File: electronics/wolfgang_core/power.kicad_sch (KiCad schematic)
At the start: 95 parts, among them IC1 LM5157RTER, J1 Power Supply, J2 Battery, J3 VXO7803-500-M-TR / ROF-78E3.3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, J4 VXO7805-500-M-TR / ROF-78E5.0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, Q1 SUM110P06-08L-E3, Q2 SUM110P06-08L-E3, Q3 SUM110P06-08L-E3, Q4 SUM110P06-08L-E3, Q5 BSS138P,215, Q6 IPD068P03L3GATMA1, SW1 power_switch, U1 LM5001MA, U2 ACS724xLCTR-50AB, U3 LTC4418IUF-PBF, U4 SN74AHCT1G08

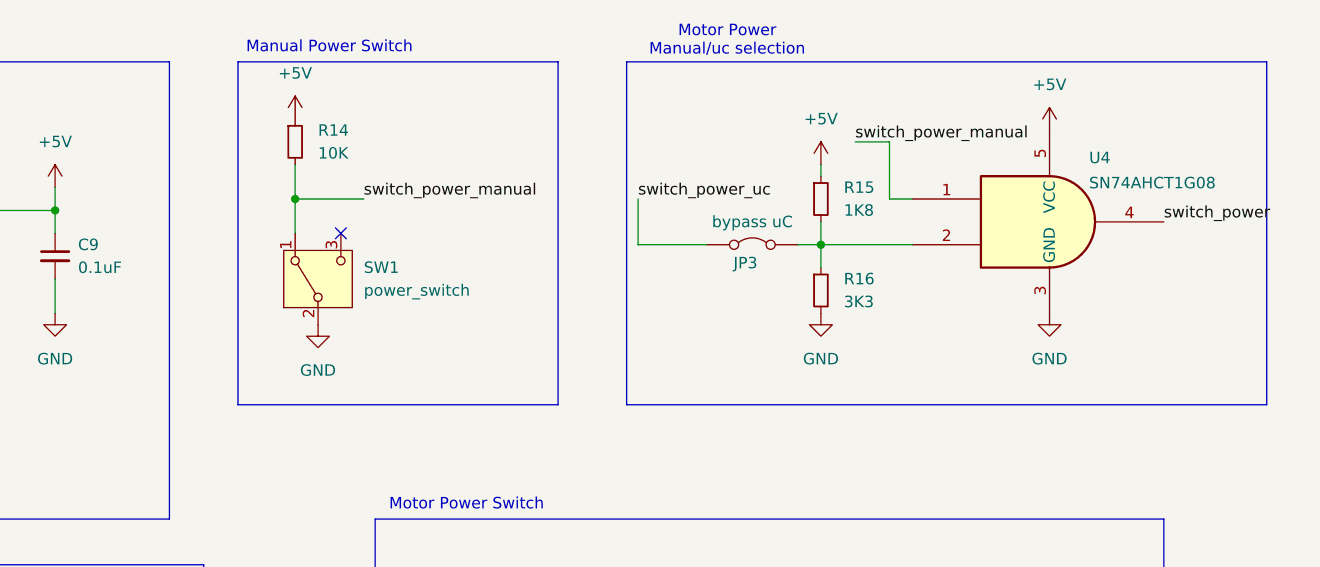
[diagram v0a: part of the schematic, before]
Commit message: Add ESP32 in io
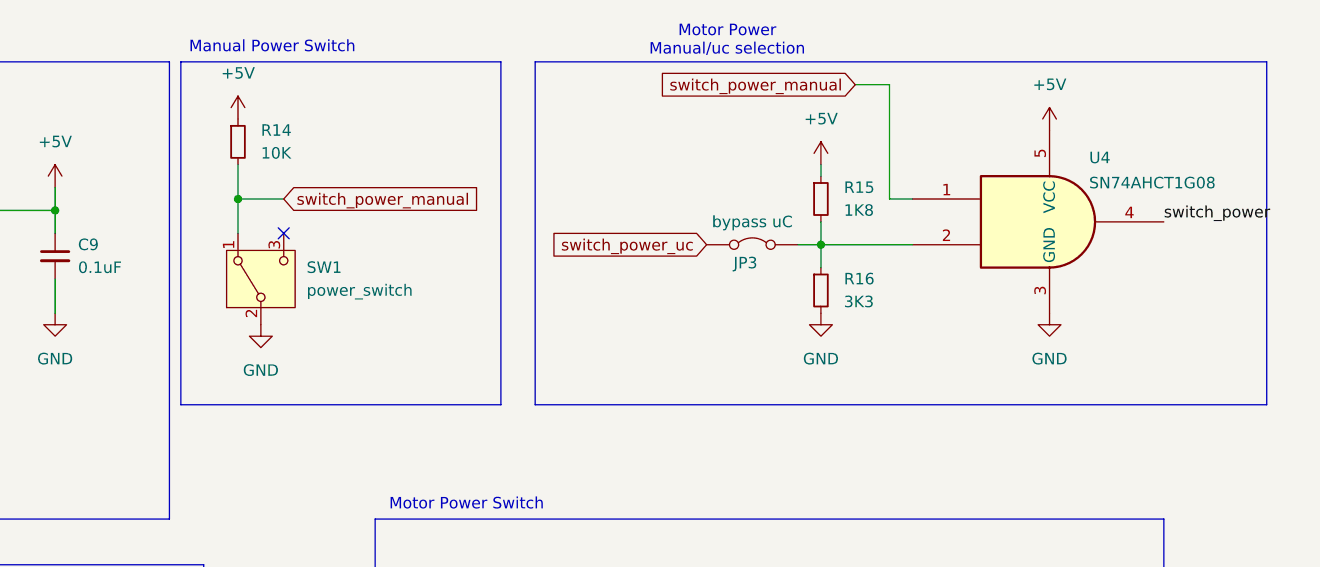
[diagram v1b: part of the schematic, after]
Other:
- moved on the sheet: R14, SW1
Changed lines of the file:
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@@
 	)
 	(junction
-		(at 293.37 33.02)
+		(at 287.02 33.02)
 		(diameter 0)
 		(color 0 0 0 0)
@@
 	)
 	(no_connect
-		(at 298.45 36.83)
+		(at 292.1 36.83)
 	)
 	(wire
@@
 	(wire
 		(pts
-			(xy 359.41 26.67) (xy 359.41 33.02)
+			(xy 359.41 20.32) (xy 359.41 33.02)
 		)
 		(stroke
@@
 	(wire
 		(pts
-			(xy 293.37 33.02) (xy 300.99 33.02)
+			(xy 287.02 33.02) (xy 292.1 33.02)
 		)
 		(stroke
@@
 	(wire
 		(pts
-			(xy 293.37 33.02) (xy 293.37 36.83)
+			(xy 287.02 33.02) (xy 287.02 36.83)
 		)
 		(stroke
@@
 	(wire
 		(pts
-			(xy 293.37 29.21) (xy 293.37 33.02)
+			(xy 287.02 29.21) (xy 287.02 33.02)
 		)
 		(stroke
@@
 	(wire
 		(pts
-			(xy 355.6 26.67) (xy 359.41 26.67)
+			(xy 355.6 20.32) (xy 359.41 20.32)
 		)
 		(stroke
@@
 	(wire
 		(pts
-			(xy 331.47 33.02) (xy 331.47 38.1)
-		)
-		(stroke
-			(width 0)
-			(type default)
-		)
-	)
-	(wire
-		(pts
 			(xy 140.97 240.03) (xy 140.97 241.3)
 		)
@@
 	(wire
 		(pts
-			(xy 331.47 38.1) (xy 339.09 38.1)
-		)
-		(stroke
-			(width 0)
-			(type default)
-		)
-	)
-	(wire
-		(pts
 			(xy 120.65 45.72) (xy 134.62 45.72)
 		)
@@
 	)
 	(rectangle
-		(start 287.02 17.78)
-		(end 322.58 55.88)
+		(start 280.67 17.78)
+		(end 316.23 55.88)
 		(stroke
 			(width 0)
@@
 	)
 	(rectangle
-		(start 330.2 17.78)
+		(start 320.04 17.78)
 		(end 401.32 55.88)
 		(stroke
@@
 	(text "Manual Power Switch"
 		(exclude_from_sim no)
-		(at 297.18 16.256 0)
+		(at 290.83 16.256 0)
 		(effects
 			(font
@@
 		)
 	)
-	(label "switch_power_manual"
-		(at 355.6 26.67 0)
-		(effects
-			(font
-				(size 1.27 1.27)
-			)
-			(justify left bottom)
-		)
-	)
 	(label "switch_power"
 		(at 306.07 99.06 0)
@@
 		)
 	)
-	(label "switch_power_manual"
-		(at 300.99 33.02 0)
+	(label "v_bat"
+		(at 33.02 40.64 0)
 		(effects
 			(font
@@
 		)
 	)
-	(label "switch_power_uc"
-		(at 331.47 33.02 0)
+	(label "v_ext"
+		(at 33.02 25.4 0)
 		(effects
 			(font
@@
 		)
 	)
-	(label "v_bat"
-		(at 33.02 40.64 0)
+	(global_label "switch_power_uc"
+		(shape input)
+		(at 339.09 38.1 180)
+		(fields_autoplaced yes)
 		(effects
 			(font
 				(size 1.27 1.27)
 			)
-			(justify left bottom)
+			(justify right)
 		)
-	)
-	(label "v_ext"
-		(at 33.02 25.4 0)
-		(effects
-			(font
-				(size 1.27 1.27)
+		(property "Intersheetrefs" "${INTERSHEET_REFS}"
+			(at 320.502 38.1 0)
+			(effects
+				(font
+					(size 1.27 1.27)
+				)
+				(justify right)
+				(hide yes)
 			)
-			(justify left bottom)
 		)
 	)
@@
 		)
 	)
+	(global_label "switch_power_manual"
+		(shape input)
+		(at 292.1 33.02 0)
+		(fields_autoplaced yes)
+		(effects
+			(font
+				(size 1.27 1.27)
+			)
+			(justify left)
+		)
+		(property "Intersheetrefs" "${INTERSHEET_REFS}"
+			(at 315.4049 33.02 0)
+			(effects
+				(font
+					(size 1.27 1.27)
+				)
+				(justify left)
+				(hide yes)
+			)
+		)
+	)
+	(global_label "switch_power_manual"
+		(shape input)
+		(at 355.6 20.32 180)
+		(fields_autoplaced yes)
+		(effects
+			(font
+				(size 1.27 1.27)
+			)
+			(justify right)
+		)
+		(property "Intersheetrefs" "${INTERSHEET_REFS}"
+			(at 332.2951 20.32 0)
+			(effects
+				(font
+					(size 1.27 1.27)
+				)
+				(justify right)
+				(hide yes)
+			)
+		)
+	)
 	(global_label "v_bat_sense"
 		(shape input)
@@
 	(symbol
 		(lib_id "power:GND")
-		(at 295.91 46.99 0)
+		(at 289.56 46.99 0)
 		(unit 1)
 		(exclude_from_sim no)
@@
 		(fields_autoplaced yes)
 		(property "Reference" "#PWR047"
-			(at 295.91 53.34 0)
+			(at 289.56 53.34 0)
 			(effects
 				(font
@@
 		)
 		(property "Value" "GND"
-			(at 295.91 52.07 0)
+			(at 289.56 52.07 0)
 			(effects
 				(font
@@
 		)
 		(property "Footprint" ""
-			(at 295.91 46.99 0)
+			(at 289.56 46.99 0)
 			(effects
 				(font
@@
 		)
 		(property "Datasheet" ""
-			(at 295.91 46.99 0)
+			(at 289.56 46.99 0)
 			(effects
 				(font
@@
 		)
 		(property "Description" "Power symbol creates a global label with name \"GND\" , ground"
-			(at 295.91 46.99 0)
+			(at 289.56 46.99 0)
 			(effects
 				(font
@@
 	(symbol
 		(lib_id "Switch:SW_SPDT")
-		(at 295.91 41.91 90)
+		(at 289.56 41.91 90)
 		(unit 1)
 		(exclude_from_sim no)
@@
 		(dnp no)
 		(property "Reference" "SW1"
-			(at 300.99 40.6399 90)
+			(at 294.64 40.6399 90)
 			(effects
 				(font
@@
 		)
 		(property "Value" "power_switch"
-			(at 300.99 43.1799 90)
+			(at 294.64 43.1799 90)
 			(effects
 				(font
@@
 		)
 		(property "Footprint" ""
-			(at 295.91 41.91 0)
+			(at 289.56 41.91 0)
 			(effects
 				(font
@@
 		)
 		(property "Datasheet" "~"
-			(at 303.53 41.91 0)
+			(at 297.18 41.91 0)
 			(effects
 				(font
@@
 		)
 		(property "Description" "Switch, single pole double throw"
-			(at 295.91 41.91 0)
+			(at 289.56 41.91 0)
 			(effects
 				(font
@@
 	(symbol
 		(lib_id "Device:R_Small")
-		(at 293.37 26.67 0)
+		(at 287.02 26.67 0)
 		(unit 1)
 		(exclude_from_sim no)
@@
 		(fields_autoplaced yes)
 		(property "Reference" "R14"
-			(at 295.91 25.3999 0)
+			(at 289.56 25.3999 0)
 			(effects
 				(font
@@
 		)
 		(property "Value" "10K"
-			(at 295.91 27.9399 0)
+			(at 289.56 27.9399 0)
 			(effects
 				(font
@@
 		)
 		(property "Footprint" ""
-			(at 293.37 26.67 0)
+			(at 287.02 26.67 0)
 			(effects
 				(font
@@
 		)
 		(property "Datasheet" "~"
-			(at 293.37 26.67 0)
+			(at 287.02 26.67 0)
 			(effects
 				(font
@@
 		)
 		(property "Description" "Resistor, small symbol"
-			(at 293.37 26.67 0)
+			(at 287.02 26.67 0)
 			(effects
 				(font
@@
 	(symbol
 		(lib_id "power:+5V")
-		(at 293.37 24.13 0)
+		(at 287.02 24.13 0)
 		(unit 1)
 		(exclude_from_sim no)
@@
 		(fields_autoplaced yes)
 		(property "Reference" "#PWR046"
-			(at 293.37 27.94 0)
+			(at 287.02 27.94 0)
 			(effects
 				(font
@@
 		)
 		(property "Value" "+5V"
-			(at 293.37 19.05 0)
+			(at 287.02 19.05 0)
 			(effects
 				(font
@@
 		)
 		(property "Footprint" ""
-			(at 293.37 24.13 0)
+			(at 287.02 24.13 0)
 			(effects
 				(font
@@
 		)
 		(property "Datasheet" ""
-			(at 293.37 24.13 0)
+			(at 287.02 24.13 0)
 			(effects
 				(font
@@
 		)
 		(property "Description" "Power symbol creates a global label with name \"+5V\""
-			(at 293.37 24.13 0)
+			(at 287.02 24.13 0)
 			(effects
 				(font

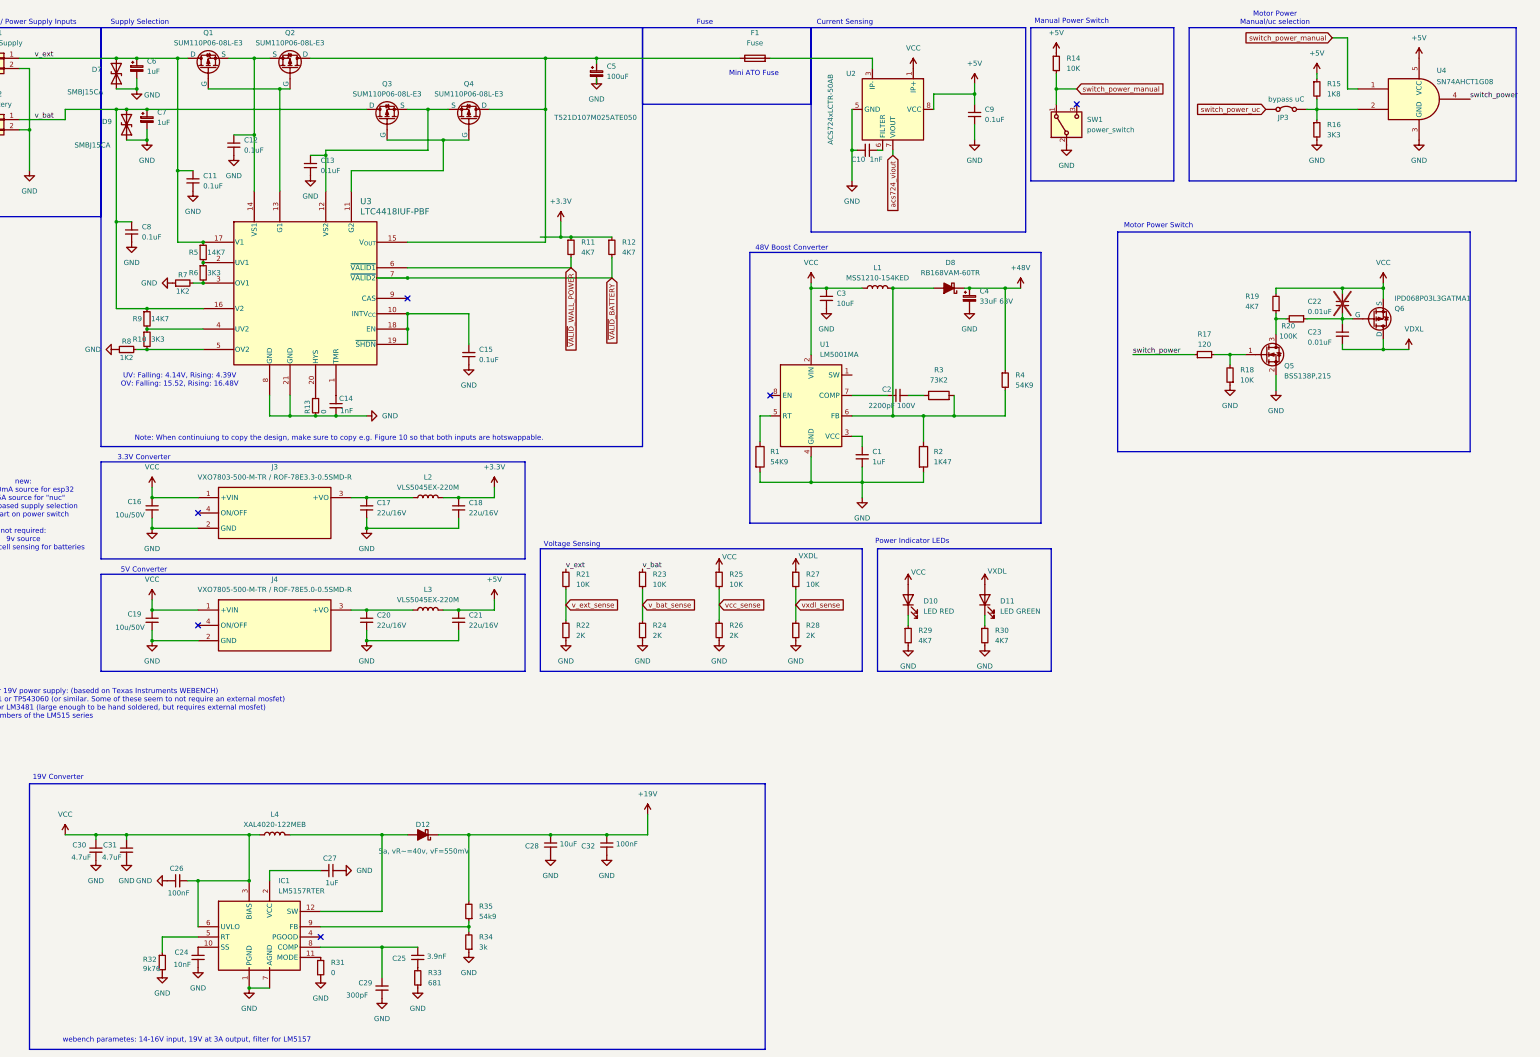
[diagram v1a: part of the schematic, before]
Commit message: Footprints hinzugefügt
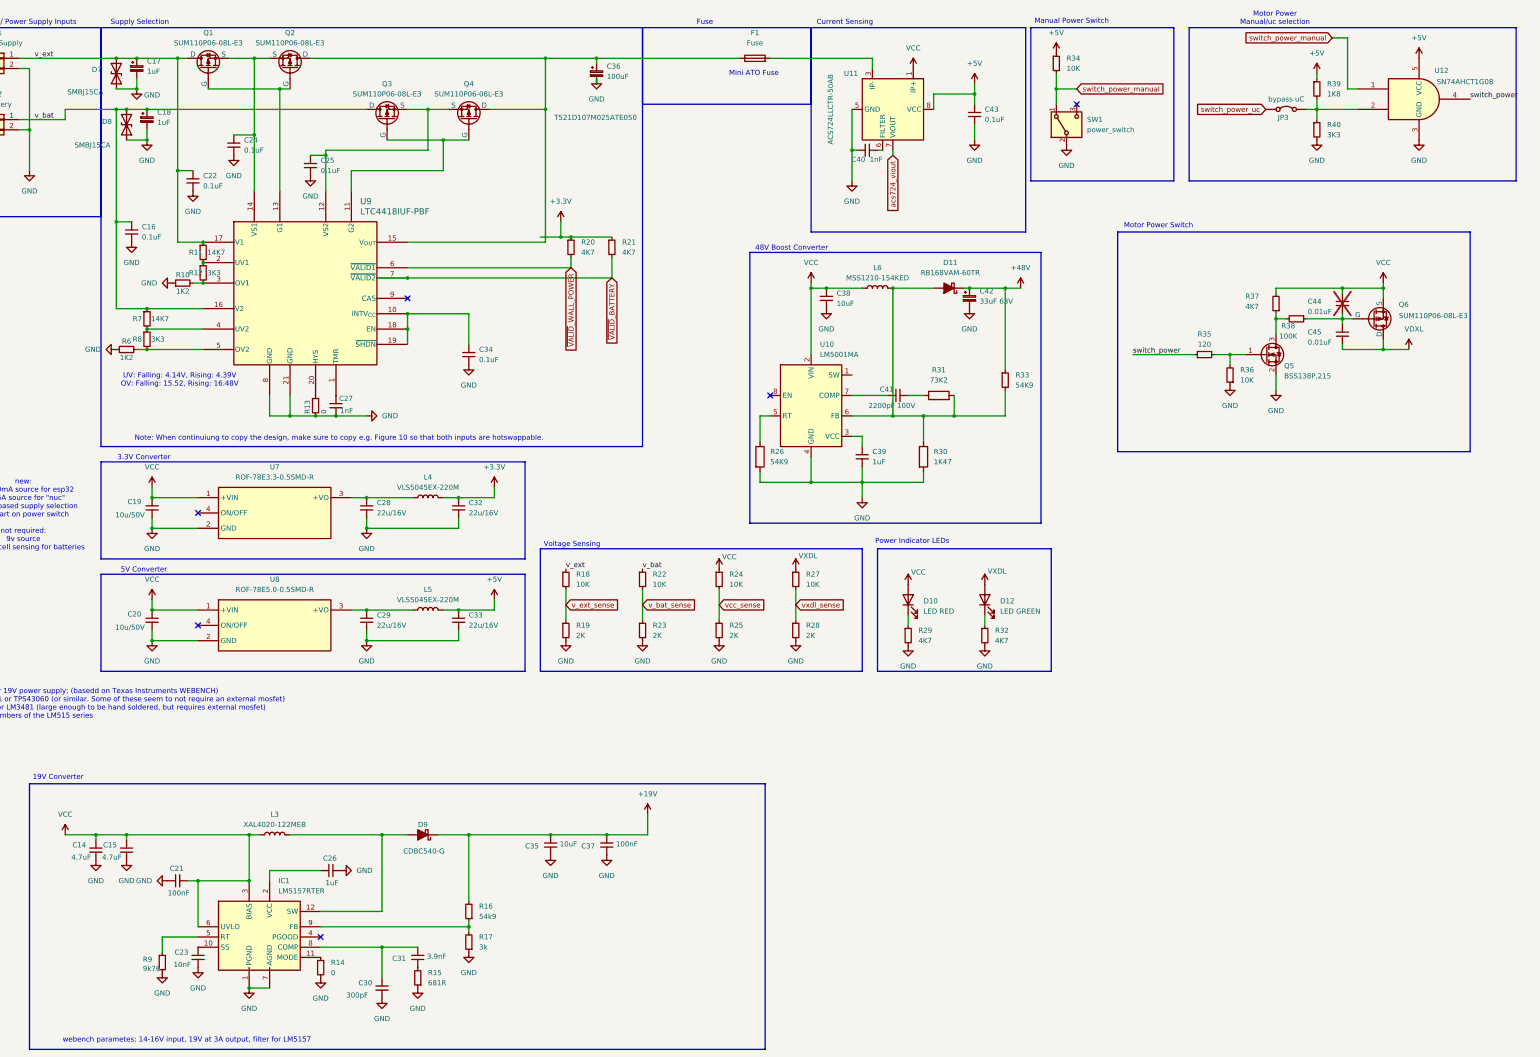
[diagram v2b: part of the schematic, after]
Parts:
- D10: footprint (none) -> LED_THT:LED_D3.0mm
- D12: renamed from D11; footprint (none) -> LED_THT:LED_D3.0mm
- D9: renamed from D12; value 5a, vR~=40v, vF=550mV -> CDBC540-G
- F1: footprint (none) -> bitbots:3557-2
- IC1: footprint QFN50P300X300X80-17N-D -> footprints:QFN50P300X300X80-17N-D
- J1, J2: footprint (none) -> Connector_AMASS:AMASS_XT60-M_1x02_P7.20mm_Vertical
- Q1, Q2, Q3, Q4: footprint (none) -> bitbots:SUM110P06-08L-E3
- Q6: value IPD068P03L3GATMA1 -> SUM110P06-08L-E3; footprint (none) -> bitbots:SUM110P06-08L-E3
- R15: renamed from R33; value 681 -> 681R
- U11: renamed from U2; value ACS724xLCTR-50AB -> ACS724LLCTR-50AB
- U7: renamed from J3; value VXO7803-500-M-TR / ROF-78E3.3-0.5SMD-R -> ROF-78E3.3-0.5SMD-R; footprint VXO7803500MTR -> footprints:VXO7803500MTR
- U8: renamed from J4; value VXO7805-500-M-TR / ROF-78E5.0-0.5SMD-R -> ROF-78E5.0-0.5SMD-R; footprint VXO7803500MTR -> footprints:VXO7803500MTR
- U9: renamed from U3; footprint UF_20_ADI -> bitbots:UF_20_ADI
- renumbered C30 to C14, C31 to C15, C8 to C16, C6 to C17, C7 to C18, C16 to C19, C19 to C20, C26 to C21, C11 to C22, C24 to C23, C12 to C24, C13 to C25, C27 to C26, C14 to C27, C17 to C28, C20 to C29, C29 to C30, C25 to C31, C18 to C32, C21 to C33, C15 to C34, C28 to C35, C5 to C36, C32 to C37, C3 to C38, C1 to C39, C10 to C40, C2 to C41, C4 to C42, C9 to C43, C22 to C44, C23 to C45, D8 to D11, D9 to D8, L4 to L3, L2 to L4, L3 to L5, L1 to L6, R7 to R10, R5 to R11, R6 to R12, R31 to R14, R35 to R16, R34 to R17, R21 to R18, R22 to R19, R11 to R20, R12 to R21, R23 to R22, R24 to R23, R25 to R24, R26 to R25, R1 to R26, R2 to R30, R3 to R31, R30 to R32, R4 to R33, R14 to R34, R17 to R35, R18 to R36, R19 to R37, R20 to R38, R15 to R39, R16 to R40, R8 to R6, R9 to R7, R10 to R8, R32 to R9, U1 to U10, U4 to U12
